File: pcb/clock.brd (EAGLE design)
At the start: 100 x 80 mm, 27 parts, among them IC1 STM32F10XCXT6, IC3 24C64ST

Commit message: rough layout
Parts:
- IC1: value STM32F10XCXT6 -> STM32F072C8T6; device stm32f072c8t6:TQFP48 -> joyAnalog:TQFP48
- moved S2 106.7 mm to (75.9, 4.83)
- moved Y1 103.7 mm to (72.9, 22.4), turned to 180 degrees
- moved Y2 100.2 mm to (64.5, 24.1), turned to 180 degrees
- moved IC1 99.9 mm to (71.1, 32.0)
- moved U$6 94.3 mm to (115.6, 8.89)
- moved U$5 54.0 mm to (95.2, 8.89)
- moved U$3 52.3 mm to (50.8, 8.89)
- moved U$4 24.4 mm to (71.1, 8.89)
- moved U$2 24.1 mm to (26.7, 8.89)
- moved U$1 19.1 mm to (6.35, 8.89)
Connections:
- new net N$1: C11.1, IC1.3, Y2.2
- new net N$2: C12.1, IC1.4, Y2.1
- new net N$3: IC1.7, R8.1, S2.1, S2.2
- new net N$5: IC1.44, R1.2
- new net N$6: C1.1, IC1.5, Y1.2
- new net N$7: C3.1, IC1.6, Y1.1
- net +3V3: now also U$1.VCC, U$2.VCC, U$3.VCC, U$4.VCC, U$5.VCC, U$6.VCC
- net GND: now also C11.2, C12.2, S2.3, S2.4, U$1.GND, U$1.GND2, U$2.GND, U$2.GND2, U$3.GND, U$3.GND2, U$4.GND, U$4.GND2, U$5.GND, U$5.GND2, U$6.GND, U$6.GND2
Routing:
- added copper zone on layer 16, net +3V3
- added copper zone on layer 1, net GND
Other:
- board size 100 x 80 mm -> 140 x 50 mm

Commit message: USBC, GPS etc
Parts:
- added CONN1: USB-C_WURTH_632723X00011USB-C, breakouts:USB-C_WURTH_632723X00011
- added SD1: TF-HOLDER, basicBoard:TF-PULL
- added U$7: MAX-M8, ubloxLib:MAX-M8
- added U$8: TEMT6000, ProtoSnap-v14a:TEMT6000-SEN
- added U$9: DS18B20, DS18B20U:MSOP8
- added X1: (no value), clock:SMA90_DIP
- moved S2 1.80 mm to (74.2, 4.57)
- moved Y2 0.92 mm to (63.8, 24.6)
- moved IC1 0.92 mm to (70.4, 32.5)
- moved U$2 0.92 mm to (25.9, 9.40)
- moved U$3 0.92 mm to (50.0, 9.40)
- moved U$4 0.92 mm to (70.4, 9.40)
- moved Y1 0.92 mm to (72.1, 22.9)
- moved U$1 0.92 mm to (5.59, 9.40)
- moved U$5 0.79 mm to (94.6, 9.40)
- moved U$6 0.79 mm to (115.0, 9.40)
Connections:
- new net 1_GND: U$7.1_GND
- new net 7_VCC_IO: U$7.7_VCC_IO
- new net 8_VCC: U$7.8_VCC
- new net 9_V_RESET_N: U$7.9_RESET_N
- new net N$4: U$7.11_RF_IN, X1.ANTENNA
- new net VDD: SD1.4
- new net VSS: SD1.6
- net GND: now also CONN1.A1, CONN1.A12, CONN1.B1, CONN1.B12, CONN1.CON1, CONN1.CON2, CONN1.CON3, CONN1.CON4, CONN1.GND1, CONN1.GND2, U$7.10_GND, U$7.12_GND, X1.GND1, X1.GND2, X1.GND3, X1.GND4

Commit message: added bake control
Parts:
- removed Y1: (no value), backplane:HC49US
- removed Y2: (no value), backplane:TC26HEZ
- added Q1: (no value), adafruit:NX3225
- added X2: (no value), adafruit:XTAL3215
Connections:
- net GND: now also Q1.2, Q1.4
- net N$1: now also Q1.1; no longer Y2.2
- net N$2: now also Q1.3; no longer Y2.1
- net N$6: now also C3.1, IC1.6, X2.P$2; no longer C1.1, IC1.5, Y1.2
- net N$7: now also C1.1, IC1.5, X2.P$1; no longer C3.1, IC1.6, Y1.1
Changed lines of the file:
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@@
 <attribute name="PROD_ID" value="SWCH-08247" x="74.168" y="4.572" size="1.778" layer="27" display="off"/>
 </element>
-<element name="Y1" library="backplane" package="HC49US" value="" x="72.136" y="22.86" rot="R180"/>
-<element name="Y2" library="backplane" package="TC26HEZ" value="" x="63.754" y="24.638" rot="R180"/>
 <element name="U$3" library="exixe_module" package="EXIXE_PAC" value="EXIXE" x="50.038" y="9.398"/>
 <element name="U$1" library="exixe_module" package="EXIXE_PAC" value="EXIXE" x="5.588" y="9.398"/>
@@
 <element name="CONN1" library="breakouts" package="USB-C_WURTH_632723X00011" value="USB-C_WURTH_632723X00011USB-C" x="48.7172" y="-1.651"/>
 <element name="SD1" library="basicBoard" package="TF-PULL" value="TF-HOLDER" x="7.62" y="29.718" rot="R90"/>
+<element name="Q1" library="adafruit" package="NX3225" value="" x="66.802" y="24.13"/>
+<element name="X2" library="adafruit" package="XTAL3215" value="" x="71.374" y="24.13" rot="R180"/>
 </elements>
 <signals>
@@
 <vertex x="0" y="0"/>
 </polygon>
-<contactref element="C11" pad="2"/>
-<contactref element="C12" pad="2"/>
 <contactref element="S2" pad="3"/>
 <contactref element="S2" pad="4"/>
@@
 <contactref element="U$7" pad="12_GND"/>
 <contactref element="U$7" pad="10_GND"/>
+<contactref element="C12" pad="2"/>
+<contactref element="C11" pad="2"/>
+<contactref element="Q1" pad="2"/>
+<contactref element="Q1" pad="4"/>
 <wire x1="68.108" y1="37.012" x2="74.858" y2="34.762" width="0" layer="19" extent="1-1"/>
 <wire x1="65.858" y1="30.262" x2="68.108" y2="37.012" width="0" layer="19" extent="1-1"/>
-<wire x1="67.658" y1="47.148" x2="68.108" y2="37.012" width="0" layer="19" extent="1-1"/>
+<wire x1="65.702" y1="24.93" x2="65.858" y2="30.262" width="0" layer="19" extent="1-1"/>
 <wire x1="50.7172" y1="7.679" x2="51.5172" y2="7.679" width="0" layer="19" extent="1-1"/>
 <wire x1="46.7172" y1="7.679" x2="45.9172" y2="7.679" width="0" layer="19" extent="1-1"/>
@@
 <contactref element="IC1" pad="1"/>
 </signal>
-<signal name="N$1">
-<contactref element="Y2" pad="2"/>
-<contactref element="IC1" pad="3"/>
-<contactref element="C11" pad="1"/>
-<wire x1="62.484" y1="24.638" x2="68.608" y2="28.012" width="0" layer="19" extent="1-1"/>
-<wire x1="-19.95" y1="31.75" x2="62.484" y2="24.638" width="0" layer="19" extent="1-1"/>
-</signal>
-<signal name="N$2">
-<contactref element="IC1" pad="4"/>
-<contactref element="Y2" pad="1"/>
-<contactref element="C12" pad="1"/>
-<wire x1="65.024" y1="24.638" x2="69.108" y2="28.012" width="0" layer="19" extent="1-1"/>
-<wire x1="-23.76" y1="31.75" x2="65.024" y2="24.638" width="0" layer="19" extent="1-1"/>
-</signal>
 <signal name="N$3">
 <contactref element="IC1" pad="7"/>
@@
 <wire x1="-25.77" y1="31.75" x2="65.858" y2="31.762" width="0" layer="19" extent="1-1"/>
 </signal>
-<signal name="N$6">
-<contactref element="IC1" pad="5"/>
-<contactref element="Y1" pad="2"/>
-<contactref element="C1" pad="1"/>
-<wire x1="69.596" y1="22.86" x2="69.608" y2="28.012" width="0" layer="19" extent="1-1"/>
-<wire x1="-33.92" y1="26.67" x2="69.608" y2="28.012" width="0" layer="19" extent="1-1"/>
-</signal>
-<signal name="N$7">
-<contactref element="IC1" pad="6"/>
-<contactref element="Y1" pad="1"/>
-<contactref element="C3" pad="1"/>
-<wire x1="74.676" y1="22.86" x2="70.108" y2="28.012" width="0" layer="19" extent="1-1"/>
-<wire x1="-37.73" y1="26.67" x2="70.108" y2="28.012" width="0" layer="19" extent="1-1"/>
-</signal>
 <signal name="9_V_RESET_N">
 <contactref element="U$7" pad="9_RESET_N"/>
@@
 <contactref element="SD1" pad="6"/>
 </signal>
+<signal name="N$6">
+<contactref element="IC1" pad="6"/>
+<contactref element="X2" pad="P$2"/>
+<contactref element="C3" pad="1"/>
+<wire x1="72.574" y1="24.13" x2="70.108" y2="28.012" width="0" layer="19" extent="1-1"/>
+<wire x1="-37.73" y1="26.67" x2="70.108" y2="28.012" width="0" layer="19" extent="1-1"/>
+</signal>
+<signal name="N$7">
+<contactref element="IC1" pad="5"/>
+<contactref element="X2" pad="P$1"/>
+<contactref element="C1" pad="1"/>
+<wire x1="70.174" y1="24.13" x2="69.608" y2="28.012" width="0" layer="19" extent="1-1"/>
+<wire x1="-33.92" y1="26.67" x2="69.608" y2="28.012" width="0" layer="19" extent="1-1"/>
+</signal>
+<signal name="N$1">
+<contactref element="IC1" pad="3"/>
+<contactref element="Q1" pad="1"/>
+<contactref element="C11" pad="1"/>
+<wire x1="65.702" y1="23.33" x2="68.608" y2="28.012" width="0" layer="19" extent="1-1"/>
+<wire x1="-19.95" y1="31.75" x2="65.702" y2="23.33" width="0" layer="19" extent="1-1"/>
+</signal>
+<signal name="N$2">
+<contactref element="IC1" pad="4"/>
+<contactref element="Q1" pad="3"/>
+<contactref element="C12" pad="1"/>
+<wire x1="67.902" y1="24.93" x2="69.108" y2="28.012" width="0" layer="19" extent="1-1"/>
+<wire x1="-23.76" y1="31.75" x2="67.902" y2="24.93" width="0" layer="19" extent="1-1"/>
+</signal>
 </signals>

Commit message: positioned boards
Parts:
- removed SD1: TF-HOLDER, basicBoard:TF-PULL
- added U$10, U$11, U$12, U$13: M3_MOUNTING_HOLE, a:M3_MOUNTING_HOLE_PACK
- moved U$8 2.72 mm to (94.5, 47.1)
- moved U$1 2.35 mm to (7.90, 9.00)
- moved U$2 2.33 mm to (28.2, 9.00)
- moved U$9 2.24 mm to (50.2, 46.7)
- moved IC1 2.20 mm to (72.5, 32.0)
- moved U$3 2.20 mm to (52.2, 9.00)
- moved U$4 2.18 mm to (72.5, 9.00)
- moved U$5 1.89 mm to (96.5, 9.00)
- moved U$6 1.87 mm to (116.8, 9.00)
- moved X1 1.70 mm to (94.4, 5.08)
- moved CONN1 1.53 mm to (50.2, -1.78)
- moved S2 1.45 mm to (75.6, 4.19)
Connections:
- removed net VDD: SD1.4
- removed net VSS: SD1.6
- net +3V3: now also U$1.3V, U$2.3V, U$3.3V, U$4.3V, U$5.3V, U$6.3V; no longer U$1.VCC, U$2.VCC, U$3.VCC, U$4.VCC, U$5.VCC, U$6.VCC
- net GND: no longer U$1.GND2, U$2.GND2, U$3.GND2, U$4.GND2, U$5.GND2, U$6.GND2
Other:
- board size 140 x 50 mm -> 145 x 50 mm

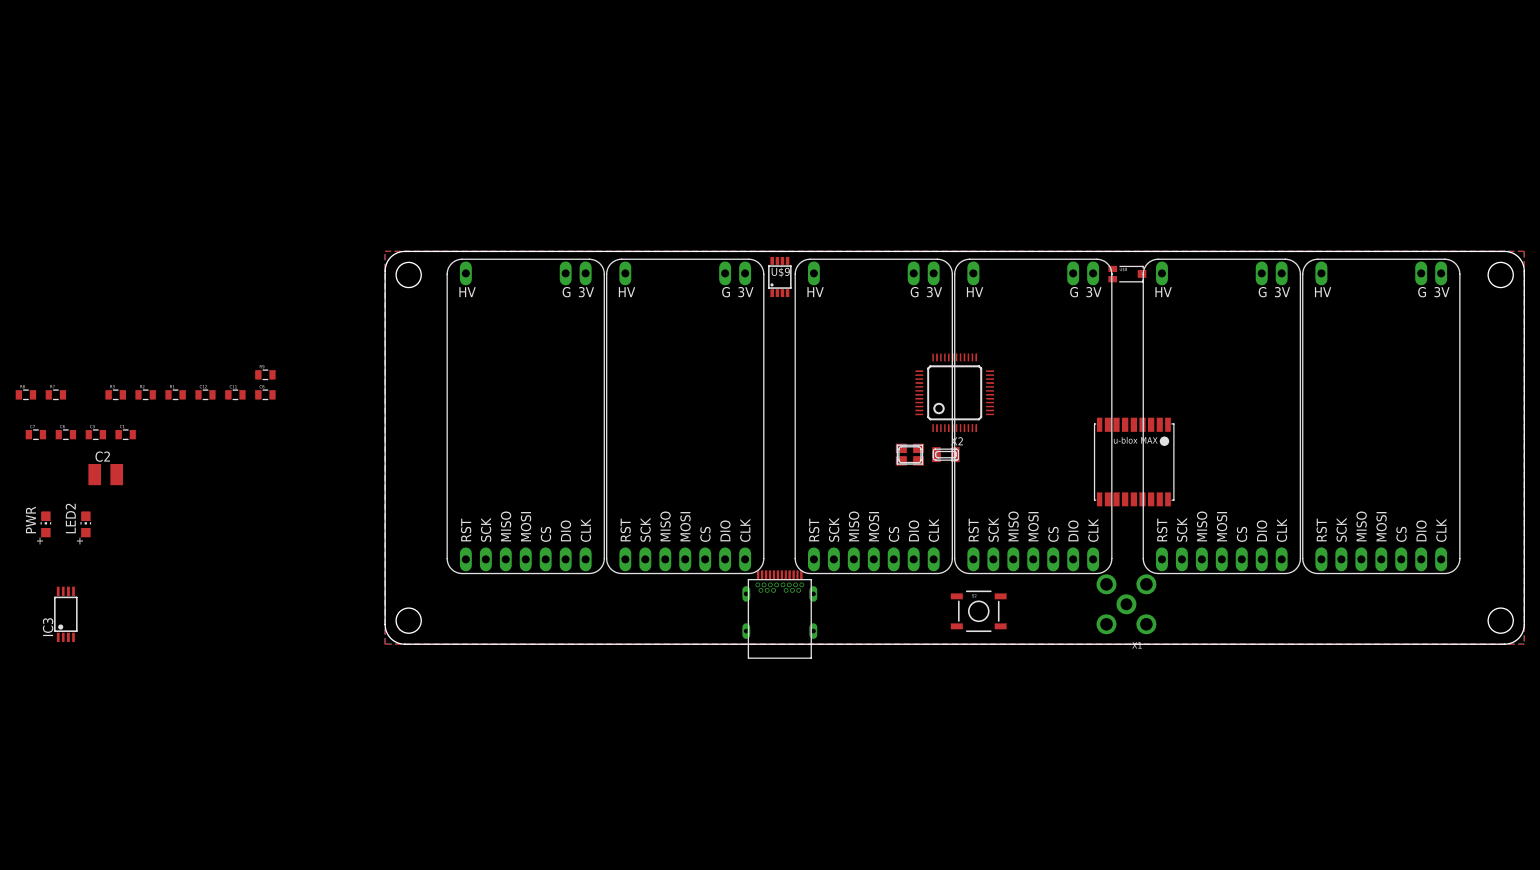
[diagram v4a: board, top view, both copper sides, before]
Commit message: added touch
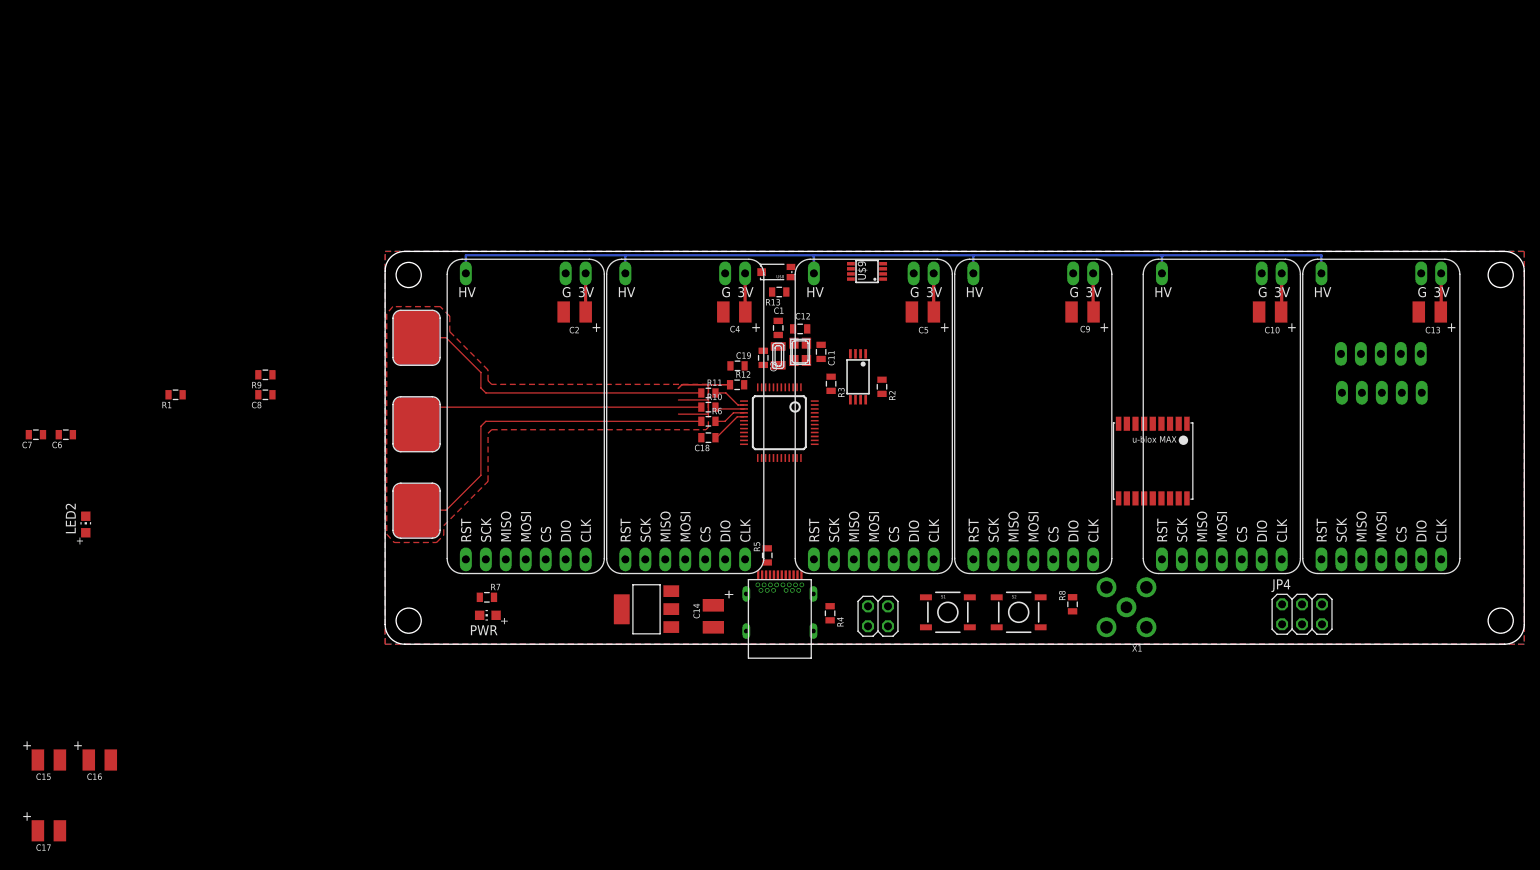
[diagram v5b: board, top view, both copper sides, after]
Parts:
- added C10, C13, C14, C15, C16, C17, C4, C5, C9: (no value), clock:C1210
- added C18, C19, R10, R11, R12, R13, R4, R5, R6: (no value), clock:0805
- added IC2: REG1117, clock:SOT223
- added JP1: (no value), nixie_power:EBAY_PKG
- added JP2: (no value), nixie_power:TAOBAO_PKG
- added JP3: (no value), pinhead:2X02
- added JP4: (no value), pinhead:2X03
- added S1: TAC_SWITCHSMD, SparkFun-Retired:TACTILE-SWITCH-SMD
- added U$14, U$15, U$16: TOUCHPAD, touch_pad:TOUCHPAD_PAK
- C1, C11, C12, C3, C6, C7, C8: device backplane:0805 -> clock:0805
- C2: device backplane:C1210 -> clock:C1210
- R1, R2, R3, R7, R8, R9: device SparkFun-Passives:0805 -> clock:0805
- moved R8 135.9 mm to (87.5, 5.08), turned to 270 degrees
- moved IC3 105.3 mm to (60.2, 34.0), turned to 180 degrees
- moved R2 93.7 mm to (63.2, 32.8), turned to 90 degrees
- moved R3 91.1 mm to (56.8, 33.1), turned to 90 degrees
- moved C3 85.5 mm to (48.1, 36.4), turned to 90 degrees
- moved C1 84.2 mm to (50.0, 40.3), turned to 90 degrees
- moved C12 76.2 mm to (52.8, 40.1)
- moved C11 74.7 mm to (55.5, 37.2), turned to 90 degrees
- moved C2 63.2 mm to (24.1, 42.3), turned to 180 degrees
- moved R7 60.6 mm to (13.0, 5.97), turned to 180 degrees
- moved PWR 57.4 mm to (13.1, 3.68), turned to 90 degrees
- moved U$8 44.7 mm to (49.8, 47.4), turned to 180 degrees
- moved X2 24.8 mm to (50.0, 36.7), turned to 90 degrees
- moved IC1 22.6 mm to (50.2, 28.2), turned to 180 degrees
- moved Q1 19.1 mm to (52.8, 37.2), turned to 90 degrees
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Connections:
- removed net 1_GND: U$7.1_GND
- new net +180V: JP1.HV, JP2.HV, U$1.HV, U$2.HV, U$3.HV, U$4.HV, U$5.HV, U$6.HV
- new net +5V: C14.1, CONN1.A4, CONN1.A9, CONN1.B4, CONN1.B9, IC2.3, JP1.5V, JP2.5V
- new net I2C_SCL: IC1.45, IC3.6, R2.1
- new net I2C_SDA: IC1.46, IC3.5, R3.1
- new net LIGHT_SENSOR_OUTPUT: R13.2, U$8.EMITTER
- new net N$10: R6.2, U$16.P$1
- new net N$11: IC1.13, R12.1
- new net N$12: CONN1.B5, R4.2
- new net N$13: CONN1.A5, R5.2
- new net N$14: R11.2, U$14.P$1
- new net N$15: IC1.15, R10.1
- new net N$16: IC1.16, R6.1
- new net N$18: C19.1, IC1.12
- new net N$8: IC1.14, R11.1
- new net N$9: R10.2, U$15.P$1
- new net NIXIE_PWR_EN: JP1.EN, JP2.EN
- new net SPI1_MISO: IC1.40
- new net SPI1_MOSI: IC1.41, U$1.MOSI, U$2.MOSI, U$3.MOSI, U$4.MOSI, U$5.MOSI, U$6.MOSI
- new net SPI1_SCK: IC1.39, U$1.SCK, U$2.SCK, U$3.SCK, U$4.SCK, U$5.SCK, U$6.SCK
- new net SWCLK: IC1.37, JP3.4
- new net SWDIO: IC1.34, JP3.2
- new net TOUCH_SENSE: C18.2, IC1.17
- new net TOUCH_SHIELD: R12.2
- new net USART1_RX: IC1.43, U$7.2_TXD
- new net USART1_TX: IC1.42, U$7.3_RXD
- new net USB_DM: CONN1.A7, CONN1.B7, IC1.32
- new net USB_DP: CONN1.A6, CONN1.B6, IC1.33
- net +3V3: now also C10.1, C13.1, C15.1, C16.1, C2.1, C4.1, C5.1, C9.1, IC2.2, IC2.4, JP3.3, S1.3, S1.4, U$8.COLLECTOR
- net GND: now also C10.2, C13.2, C14.2, C15.2, C16.2, C18.1, C19.2, C2.2, C4.2, C5.2, C9.2, IC2.1, IC3.1, IC3.2, IC3.3, IC3.7, JP1.GND, JP1.GND2, JP2.GND, JP2.GND2, JP3.1, R1.2, R13.1, R4.1, R5.1, U$7.1_GND; no longer R1.1
- net N$5: now also R1.1, S1.1, S1.2; no longer R1.2
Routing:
- net +180V: track 0.00 -> 122.9 mm
- net N$10: track 0.00 -> 44.6 mm
- net N$14: track 0.00 -> 40.3 mm
- net N$9: track 0.00 -> 37.1 mm
- net +3V3: track 0.00 -> 29.6 mm
- net TOUCH_SHIELD: track 0.00 -> 18.1 mm
- net TOUCH_SENSE: track 0.00 -> 4.74 mm
- net N$8: track 0.00 -> 4.27 mm
- net N$16: track 0.00 -> 4.08 mm
- net N$15: track 0.00 -> 3.73 mm
- added copper zone on layer 1, net TOUCH_SHIELD

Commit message: routing
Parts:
- removed C15, C16: (no value), clock:C1210
- removed CONN1: USB-C_WURTH_632723X00011USB-C, breakouts:USB-C_WURTH_632723X00011
- added L1: (no value), basicBoard:0805
- added R14, R15: (no value), clock:0805
- added X3: USB-MICROB, basicBoard:USB-MICROB
- C17: device clock:C1210 -> clock:0805
- moved C17 148.9 mm to (100.8, 15.4), turned to 90 degrees
- moved C7 98.0 mm to (53.3, 20.2), turned to 270 degrees
- moved R1 95.1 mm to (64.3, 3.94), turned to 270 degrees
- moved JP2 52.7 mm to (77.2, 19.1), turned to 180 degrees
- moved JP1 50.3 mm to (77.2, 23.9), turned to 180 degrees
- moved R4 43.4 mm to (98.5, 15.4), turned to 270 degrees
- moved R5 13.7 mm to (57.1, 22.1)
- moved R8 10.7 mm to (76.9, 3.94)
- moved JP3 3.34 mm to (59.4, 4.06)
- moved S2 2.27 mm to (82.7, 5.08)
- moved S1 2.27 mm to (69.6, 5.08)
- moved C14 1.65 mm to (41.8, 5.21)
- moved U$7 0.31 mm to (97.7, 23.4)
- moved X1 0.28 mm to (94.5, 4.45)
- moved IC2 0.13 mm to (33.3, 4.32)
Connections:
- new net EXIXE_RESET: IC1.38, U$1.RST, U$2.RST, U$3.RST, U$4.RST, U$5.RST, U$6.RST
- new net N$17: IC1.39, R5.1
- new net N$19: IC1.41, R15.1
- new net N$20: IC1.40, R14.1
- net +3V3: no longer C15.1, C16.1
- net +5V: now also X3.VBUS; no longer CONN1.A4, CONN1.A9, CONN1.B4, CONN1.B9
- net GND: now also C17.2, X3.GND, X3.P1, X3.P2, X3.P3, X3.P4, X3.P5, X3.P6; no longer C15.2, C16.2, CONN1.A1, CONN1.A12, CONN1.B1, CONN1.B12, CONN1.CON1, CONN1.CON2, CONN1.CON3, CONN1.CON4, CONN1.GND1, CONN1.GND2, R4.1, R5.1
- net N$12: now also C17.1, L1.2; no longer CONN1.B5
- net N$13: now also R4.1, U$7.14_VCC_RF; no longer CONN1.A5, R5.2
- net N$4: now also L1.1
- net SPI1_MISO: now also R14.2, U$1.MISO, U$2.MISO, U$3.MISO, U$4.MISO, U$5.MISO, U$6.MISO; no longer IC1.40
- net SPI1_MOSI: now also R15.2; no longer IC1.41
- net SPI1_SCK: now also R5.2; no longer IC1.39
- net USART1_RX: now also U$7.3_RXD; no longer U$7.2_TXD
- net USART1_TX: now also U$7.2_TXD; no longer U$7.3_RXD
- net USB_DM: now also X3.D-; no longer CONN1.A7, CONN1.B7
- net USB_DP: now also X3.D+; no longer CONN1.A6, CONN1.B6
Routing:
- net SPI1_MISO: track 0.00 -> 194.2 mm
- net SPI1_MOSI: track 0.00 -> 191.2 mm
- net EXIXE_RESET: track 0.00 -> 164.7 mm
- net SPI1_SCK: track 0.00 -> 155.3 mm
- net N$3: track 0.00 -> 64.6 mm
- net USART1_TX: track 0.00 -> 49.0 mm
- net USART1_RX: track 0.00 -> 47.4 mm
- net N$5: track 0.00 -> 47.0 mm
- net +180V: track 122.9 -> 158.6 mm
- net SWCLK: track 0.00 -> 27.9 mm
- net +5V: track 0.00 -> 25.6 mm
- net SWDIO: track 0.00 -> 22.8 mm
- net +3V3: track 29.6 -> 51.4 mm, vias 0 -> 5
- net USB_DM: track 0.00 -> 20.2 mm
- net USB_DP: track 0.00 -> 20.1 mm
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
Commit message: routing done
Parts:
- removed JP4: (no value), pinhead:2X03
- added G1: CH291-1220LF, basicBoard:CH291-1220LF
- added JP5: (no value), pinhead:1X04
- added R16: (no value), clock:0805
- added S4, S5: SWITCH-MOMENTARY-2SIDE_EZ, bus:TACTILE-PTH-SIDEEZ
- added TP1: PTR1TP20R, testpad:TP20R
- moved PWR 117.5 mm to (130.6, 3.81)
- moved R7 116.5 mm to (129.4, 6.99)
- moved C6 85.3 mm to (44.6, 22.9), turned to 225 degrees
- moved C8 71.6 mm to (56.4, 31.9), turned to 90 degrees
- moved LED2 65.5 mm to (26.5, 4.57), turned to 180 degrees
- moved R9 48.9 mm to (21.5, 2.03), turned to 180 degrees
- moved JP2 4.82 mm to (72.6, 20.6)
- moved JP1 4.82 mm to (72.6, 25.4)
- moved R3 2.29 mm to (58.7, 31.9)
- moved C14 2.04 mm to (41.9, 3.17)
- moved IC3 1.31 mm to (61.3, 33.4)
- moved R2 1.09 mm to (63.9, 31.9), turned to 270 degrees
- moved IC2 0.90 mm to (33.4, 3.43)
- moved C3 0.81 mm to (47.6, 37.1)
- moved U$8 0.80 mm to (50.0, 48.1)
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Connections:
- removed net 7_VCC_IO: U$7.7_VCC_IO
- removed net 8_VCC: U$7.8_VCC
- removed net 9_V_RESET_N: U$7.9_RESET_N
- removed net VDDA: IC1.9
- removed net VSSA: IC1.8
- new net DS18B20_DATA: IC1.2, R16.1, U$9.1
- new net EXIXE1_CS: IC1.18, U$1.CS
- new net EXIXE2_CS: IC1.19, U$2.CS
- new net EXIXE3_CS: IC1.20, U$3.CS
- new net EXIXE4_CS: IC1.25, U$4.CS
- new net EXIXE5_CS: IC1.26, U$5.CS
- new net EXIXE6_CS: IC1.27, U$6.CS
- new net GPS_RESET: IC1.10, U$7.9_RESET_N
- new net GPS_TP: IC1.28, U$7.4_TIMEPULSE
- new net N$21: LED2.C, R9.1
- new net N$22: IC1.31, S4.1
- new net N$23: IC1.29, S5.1
- new net RX3: IC1.21, JP5.1
- new net TX3: IC1.22, JP5.2, R9.2
- net +3V3: now also IC1.9, JP5.4, LED2.A, R16.2, U$7.7_VCC_IO, U$7.8_VCC, U$9.8
- net GND: now also G1.-, IC1.8, JP5.3, S4.2, S4.ANCHOR1, S4.ANCHOR2, S5.2, S5.ANCHOR1, S5.ANCHOR2, U$9.4
- net LIGHT_SENSOR_OUTPUT: now also IC1.11
- net VBAT: now also G1.+, U$7.6_V_BCKP
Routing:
- net GND: track 15.9 -> 167.9 mm, vias 0 -> 1
- net N$23: track 0.00 -> 126.5 mm, vias 0 -> 2
- net N$22: track 0.00 -> 109.2 mm, vias 0 -> 2
- net EXIXE6_CS: track 0.00 -> 105.1 mm, vias 0 -> 2
- net EXIXE5_CS: track 0.00 -> 85.6 mm, vias 0 -> 2
- net VBAT: track 0.00 -> 84.8 mm, vias 0 -> 2
- net GPS_TP: track 0.00 -> 65.6 mm, vias 0 -> 2
- net GPS_RESET: track 0.00 -> 65.2 mm, vias 0 -> 2
- net EXIXE4_CS: track 0.00 -> 53.3 mm, vias 0 -> 2
- net TX3: track 0.00 -> 51.9 mm
- net RX3: track 0.00 -> 47.9 mm
- net EXIXE1_CS: track 0.00 -> 37.9 mm
- net EXIXE3_CS: track 0.00 -> 35.4 mm, vias 0 -> 2
- net +5V: track 25.6 -> 60.7 mm, vias 0 -> 2
- net +3V3: track 51.4 -> 80.5 mm, vias 5 -> 11
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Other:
- board text added: "1"
- board text added: "2"
- board text added: "3"
- board text added: "4"
- board text added: "5"
- board text added: "6"
